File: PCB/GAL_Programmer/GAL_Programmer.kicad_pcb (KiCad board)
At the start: 2 copper layers, 68.6 x 53.3 mm, 21 parts, among them P1 Power, P2 Analog, P3 Digital, P4 Digital, P5 CONN_01X01, P6 CONN_01X01, P7 CONN_01X01, P8 CONN_01X01, U1 ATF16V8, U2 ATF22V10, U3 MT3608

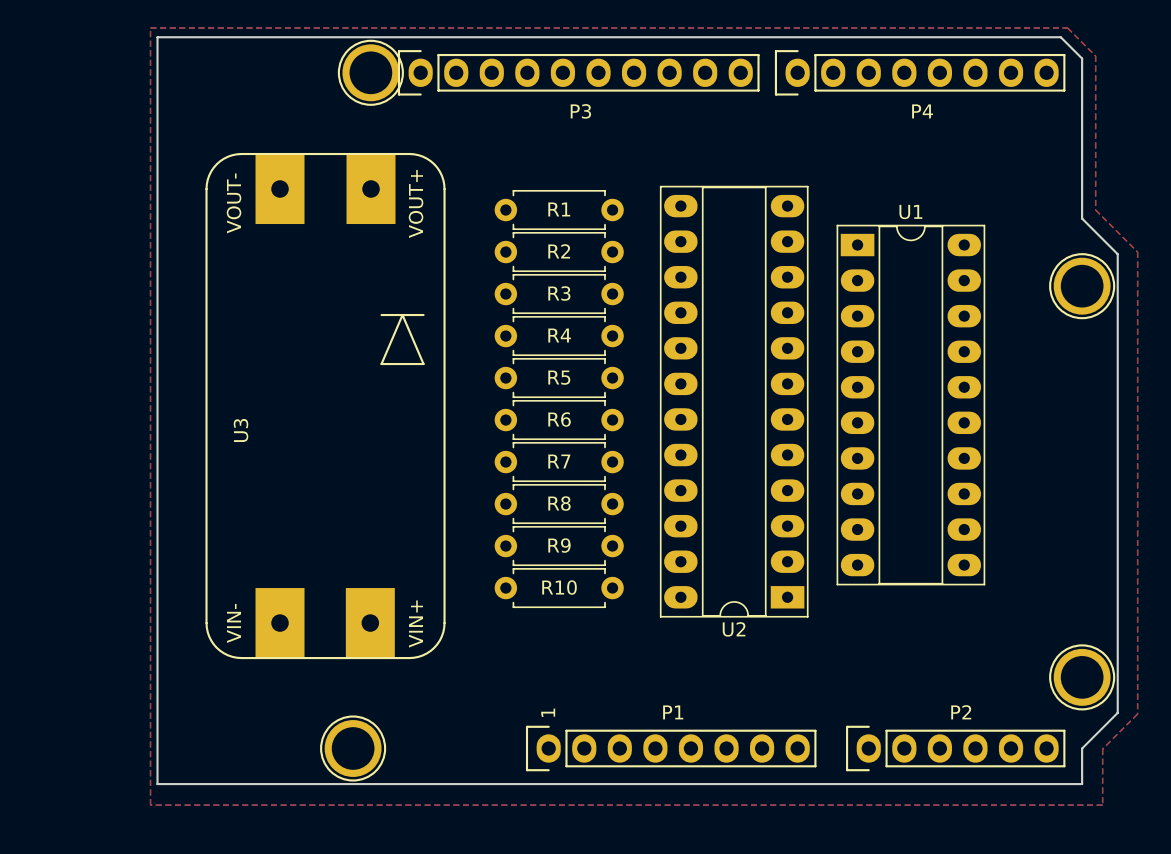
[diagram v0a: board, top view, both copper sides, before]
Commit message: Se agregaron capacitores al esquematico y al PCB, esta por empezar el ruteo del PCB
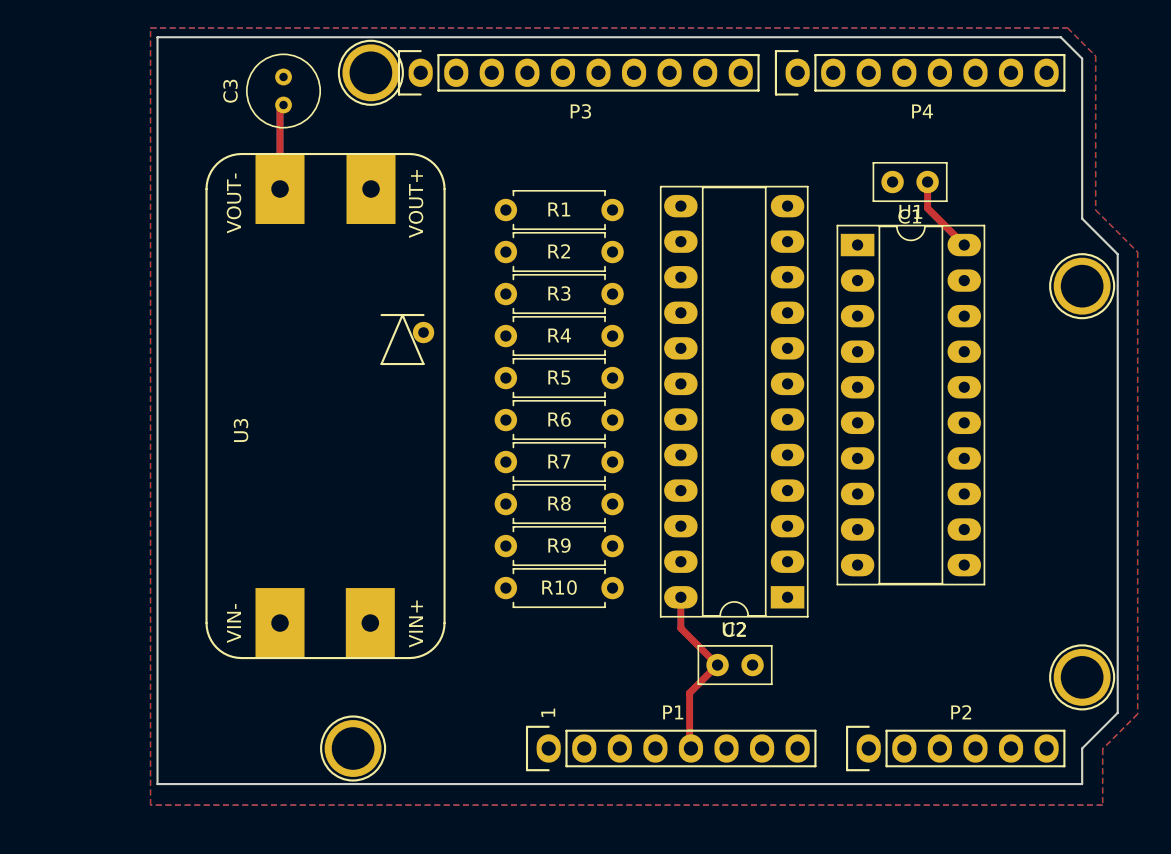
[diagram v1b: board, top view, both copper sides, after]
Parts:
- added C1: 100nf, Capacitor_THT:C_Disc_D5.0mm_W2.5mm_P2.50mm, F.Cu at (166.0, 83.4)
- added C2: 100nf, Capacitor_THT:C_Disc_D5.0mm_W2.5mm_P2.50mm, F.Cu at (151.0, 117.9)
- added C3: 10uf, Capacitor_THT:C_Radial_D5.0mm_H7.0mm_P2.00mm, F.Cu at (120.0, 77.9)
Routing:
- net +5V: track 0.00 -> 18.3 mm
- net /EDIT: track 0.00 -> 6.10 mm
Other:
- net class Default: trace_width 0.25 -> 0.3
- net class PWR added: clearance 0.2, trace_width 0.5, via_dia 0.6, via_drill 0.4

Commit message: Interfaz: Se terminaron los background workers, todos fueron probados y funcionaron correctamente, se creo el empaquetado del instalador, falta probar con alguien mas para liberar el primer versión, se hicieron cambios de estetica, en colores de botones, se agrego la función al momento de presionar el boton de DESCONECTAR, se reinicien los colores de todos los botones y el progress bar. La interfaz esta lista y funcional. Programa el GAL16V8 sin problemas, el 22V10 tiene problemas que no lo detecta como tal pero si funciona la programación. Se agregaron iconos de circuitos intergados a la interfaz
PCB: Se termino el listado de componentes, el ruteado y se pudo agregar el socket ZIF para 20 y 24 pines, todo el ruteado se completo sin problemas y en orden, se tuvo que agrandar el PCB ya que la fuente CD/CD no cabia por el tamaño de los socket ZIF. Falta agregar información de la construcción y detalles esteticos. Queda pendiente probar con Arduino Leonardo y hacer una prueba de funcionamiento, esto serviría para los programadores como standalone que podrían usarse fijamente.
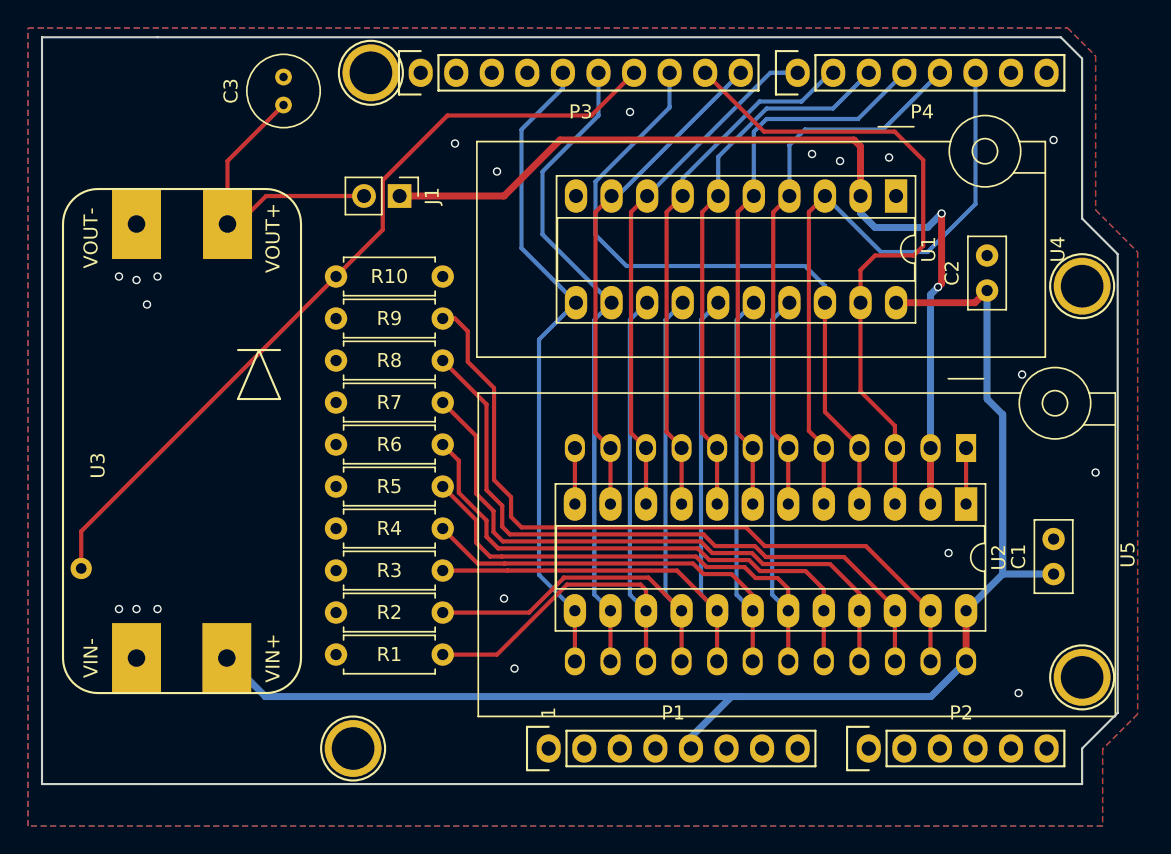
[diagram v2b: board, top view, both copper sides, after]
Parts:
- added J1: Conn_01x02_Male, Connector_PinHeader_2.54mm:PinHeader_1x02_P2.54mm_Vertical, F.Cu at (128.3, 84.4)
- added U4: ATF16V8, Socket:DIP_Socket-20_W4.3_W5.08_W7.62_W10.16_W10.9_3M_220-3342-00-0602J, F.Cu at (163.7, 84.4)
- added U5: ATF22V10, Socket:DIP_Socket-24_W11.9_W12.7_W15.24_W17.78_W18.5_3M_224-1275-00-0602J, F.Cu at (168.7, 102.4)
- moved C2 33.0 mm to (170.2, 91.1), turned to 90 degrees
- moved R1 32.1 mm to (131.4, 117.1), turned to 180 degrees
- moved C1 29.4 mm to (175.0, 111.4), turned to 90 degrees
- moved R2 26.1 mm to (131.4, 114.1), turned to 180 degrees
- moved R10 25.3 mm to (123.7, 90.1)
- moved R3 20.3 mm to (131.4, 111.1), turned to 180 degrees
- moved R9 16.9 mm to (131.4, 93.1), turned to 180 degrees
- moved R4 14.5 mm to (131.4, 108.1), turned to 180 degrees
- moved U2 14.4 mm to (168.7, 106.4), turned to 270 degrees
- moved R8 11.2 mm to (131.4, 96.1), turned to 180 degrees
- moved U3 10.6 mm to (112.7, 103.4)
- moved R5 8.97 mm to (131.4, 105.1), turned to 180 degrees
- moved R7 6.20 mm to (131.4, 99.1), turned to 180 degrees
- moved R6 4.84 mm to (131.4, 102.1), turned to 180 degrees
- moved U1 4.45 mm to (163.7, 84.4), turned to 270 degrees
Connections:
- net Net-(R1-Pad1) renamed /R1
- net Net-(R2-Pad1) renamed /R2
- net Net-(R3-Pad1) renamed /R3
- net Net-(R4-Pad1) renamed /R4
- net Net-(R5-Pad1) renamed /R5
- net Net-(R6-Pad1) renamed /R6
- net Net-(R7-Pad1) renamed /R7
- net Net-(R8-Pad1) renamed /R8
- net Net-(R9-Pad1) renamed /R9
- C3 pad 1: /EDIT -> Net-(C3-Pad1)
- P2 pad 5: /A4(SDA) -> Net-(P2-Pad5)
- P2 pad 6: /A5(SCL) -> Net-(P2-Pad6)
- P3 pad 1: /A5(SCL) -> Net-(P3-Pad1)
- P3 pad 2: /A4(SDA) -> Net-(P3-Pad2)
- U3 pad 3: /EDIT -> Net-(C3-Pad1)
- U3 pad 5: (no net) -> /11(MOSI)
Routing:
- net +5V: track 18.3 -> 99.2 mm
- net /EDIT: track 6.10 -> 67.2 mm, vias 0 -> 2
- net /11(MOSI): track 0.00 -> 57.8 mm
- net /R5: track 0.00 -> 56.8 mm
- net /R9: track 0.00 -> 53.1 mm
- net /R4: track 0.00 -> 51.8 mm
- net /10(**/SS): track 0.00 -> 48.3 mm
- net /R8: track 0.00 -> 47.9 mm
- net /R3: track 0.00 -> 47.4 mm
- net /9(**): track 0.00 -> 47.2 mm
- net /13(SCK): track 0.00 -> 47.0 mm
- net /12(MISO): track 0.00 -> 46.8 mm
- net /2: track 0.00 -> 46.1 mm
- net /R2: track 0.00 -> 45.7 mm
- net /R1: track 0.00 -> 44.8 mm
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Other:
- board size 68.6 x 53.3 mm -> 76.8 x 53.3 mm

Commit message: Todos los archivos para producción fueron generados, el PCB esta listo para ser fabricado. Se revisaron los detalles pendientes y se completo la revisión final.
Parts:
- added G***: LOGO, logos:FIME7, F.Cu at (130.6, 121.7)
- added G***: LOGO, logos:FIME6, B.Cu at (106.8, 77.0)
- added G***: LOGO, logos:FIME2, B.Cu at (142.8, 100.8)
- moved C3 3.09 mm to (120.7, 80.9)
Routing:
- net Net-(C3-Pad1): track 20.7 -> 17.7 mm
- net /13(SCK): track 47.0 -> 49.7 mm
- net GND: vias 20 -> 35
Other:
- board text added: "Nov 2021"
- board text added: "Programador GAL v1.0.0"
- board text removed: "1"
